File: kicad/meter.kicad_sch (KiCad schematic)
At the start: 10 parts, among them U10 MAX7219, U9 MAX7219

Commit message: kicad updates
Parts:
- added BAR1, BAR2, BAR3, BAR4, BAR5, BAR6, BAR7, BAR8: HDSP-4832_2, Display:HDSP-4832, symbol LED:HDSP-4832_2
- added C1, C12, C13, C2: 100nF, Capacitor_THT:C_Axial_L5.1mm_D3.1mm_P7.50mm_Horizontal, symbol Device:C
- added R1, R2, R3, R4: R, Resistor_THT:R_Axial_DIN0207_L6.3mm_D2.5mm_P10.16mm_Horizontal, symbol Device:R
- added U11: RED, Package_DIP:DIP-24_W7.62mm_Socket, symbol Driver_LED:MAX7219
- added U12: YELLOW, Package_DIP:DIP-24_W7.62mm_Socket, symbol Driver_LED:MAX7219
- U10: value MAX7219 -> GREEN_LOWER; footprint (none) -> Package_DIP:DIP-24_W7.62mm_Socket
- U9: value MAX7219 -> GREEN_UPPER; footprint (none) -> Package_DIP:DIP-24_W7.62mm_Socket
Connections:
- net CLK2 is gone; now on net CLK: U10.13 (CLK)
- net LOAD2 is gone; now on net LOAD: U10.12 (LOAD)
- net +5V: now also C1.2, C12.2, C13.2, C2.2, U11.19 (V+), U12.19 (V+); no longer U10.18 (ISET), U9.18 (ISET)
- net GND: now also C1.1, C12.1, C13.1, C2.1, R1.1, R2.1, R3.1, R4.1, U11.4 (GND), U11.9 (GND), U12.4 (GND), U12.9 (GND); no longer U10.24 (DOUT), U9.24 (DOUT)
- net at U9.20 (SEG_C): now also BAR10.18 (K), BAR11.18 (K), BAR12.18 (K), BAR13.18 (K), BAR14.18 (K), BAR15.18 (K), BAR16.18 (K), BAR9.18 (K)
- net at U9.21 (SEG_E): now also BAR10.16 (K), BAR11.16 (K), BAR12.16 (K), BAR13.16 (K), BAR14.16 (K), BAR15.16 (K), BAR16.16 (K), BAR9.16 (K)
- net at U9.23 (SEG_D): now also BAR10.17 (K), BAR11.17 (K), BAR12.17 (K), BAR13.17 (K), BAR14.17 (K), BAR15.17 (K), BAR16.17 (K), BAR9.17 (K)
- net CLK1 renamed CLK
- net CLK: now also U11.13 (CLK), U12.13 (CLK)
- net DIN1: no longer names the net of U9.1 (DIN)
- net DIN1: now also U12.24 (DOUT)
- net DIN2: no longer names the net of U10.1 (DIN)
- net DIN2: now also U9.24 (DOUT)
- net LOAD1 renamed LOAD
- net LOAD: now also U11.12 (LOAD), U12.12 (LOAD)
- new net: BAR14.10 (A), BAR14.6 (A), BAR14.7 (A), BAR14.8 (A), BAR14.9 (A), U10.10 (DIG_5)
- new net: BAR10.10 (A), BAR10.6 (A), BAR10.7 (A), BAR10.8 (A), BAR10.9 (A), U10.11 (DIG_1)
- new net: BAR10.15 (K), BAR11.15 (K), BAR12.15 (K), BAR13.15 (K), BAR14.15 (K), BAR15.15 (K), BAR16.15 (K), BAR9.15 (K), U10.14 (SEG_A)
- new net: BAR10.14 (K), BAR11.14 (K), BAR12.14 (K), BAR13.14 (K), BAR14.14 (K), BAR15.14 (K), BAR16.14 (K), BAR9.14 (K), U10.16 (SEG_B)
- new net: R2.2, U10.18 (ISET)
- new net: BAR9.10 (A), BAR9.6 (A), BAR9.7 (A), BAR9.8 (A), BAR9.9 (A), U10.2 (DIG_0)
- new net: BAR10.13 (K), BAR11.13 (K), BAR12.13 (K), BAR13.13 (K), BAR14.13 (K), BAR15.13 (K), BAR16.13 (K), BAR9.13 (K), U10.20 (SEG_C)
- new net: BAR10.11 (K), BAR11.11 (K), BAR12.11 (K), BAR13.11 (K), BAR14.11 (K), BAR15.11 (K), BAR16.11 (K), BAR9.11 (K), U10.21 (SEG_E)
- new net: BAR10.12 (K), BAR11.12 (K), BAR12.12 (K), BAR13.12 (K), BAR14.12 (K), BAR15.12 (K), BAR16.12 (K), BAR9.12 (K), U10.23 (SEG_D)
- new net: BAR13.10 (A), BAR13.6 (A), BAR13.7 (A), BAR13.8 (A), BAR13.9 (A), U10.3 (DIG_4)
- new net: BAR15.10 (A), BAR15.6 (A), BAR15.7 (A), BAR15.8 (A), BAR15.9 (A), U10.5 (DIG_6)
- new net: BAR11.10 (A), BAR11.6 (A), BAR11.7 (A), BAR11.8 (A), BAR11.9 (A), U10.6 (DIG_2)
- new net: BAR12.10 (A), BAR12.6 (A), BAR12.7 (A), BAR12.8 (A), BAR12.9 (A), U10.7 (DIG_3)
- new net: BAR16.10 (A), BAR16.6 (A), BAR16.7 (A), BAR16.8 (A), BAR16.9 (A), U10.8 (DIG_7)
- new net: BAR14.1 (A), BAR14.2 (A), BAR14.3 (A), BAR14.4 (A), BAR14.5 (A), U9.10 (DIG_5)
- new net: BAR10.1 (A), BAR10.2 (A), BAR10.3 (A), BAR10.4 (A), BAR10.5 (A), U9.11 (DIG_1)
- new net: BAR10.20 (K), BAR11.20 (K), BAR12.20 (K), BAR13.20 (K), BAR14.20 (K), BAR15.20 (K), BAR16.20 (K), BAR9.20 (K), U9.14 (SEG_A)
- new net: BAR10.19 (K), BAR11.19 (K), BAR12.19 (K), BAR13.19 (K), BAR14.19 (K), BAR15.19 (K), BAR16.19 (K), BAR9.19 (K), U9.16 (SEG_B)
- new net: R1.2, U9.18 (ISET)
- new net: BAR9.1 (A), BAR9.2 (A), BAR9.3 (A), BAR9.4 (A), BAR9.5 (A), U9.2 (DIG_0)
- new net: BAR13.1 (A), BAR13.2 (A), BAR13.3 (A), BAR13.4 (A), BAR13.5 (A), U9.3 (DIG_4)
- new net: BAR15.1 (A), BAR15.2 (A), BAR15.3 (A), BAR15.4 (A), BAR15.5 (A), U9.5 (DIG_6)
- new net: BAR11.1 (A), BAR11.2 (A), BAR11.3 (A), BAR11.4 (A), BAR11.5 (A), U9.6 (DIG_2)
- new net: BAR12.1 (A), BAR12.2 (A), BAR12.3 (A), BAR12.4 (A), BAR12.5 (A), U9.7 (DIG_3)
- new net: BAR16.1 (A), BAR16.2 (A), BAR16.3 (A), BAR16.4 (A), BAR16.5 (A), U9.8 (DIG_7)
- new net: BAR3.1 (A), BAR3.2 (A), BAR3.3 (A), BAR3.4 (A), BAR3.5 (A), U11.6 (DIG_2)
- new net: BAR3.10 (A), BAR3.6 (A), BAR3.7 (A), BAR3.8 (A), BAR3.9 (A), U12.6 (DIG_2)
- new net: BAR1.11 (K), BAR2.11 (K), BAR3.11 (K), BAR4.11 (K), BAR5.11 (K), BAR6.11 (K), BAR7.11 (K), BAR8.11 (K), U12.21 (SEG_E)
- new net: BAR1.12 (K), BAR2.12 (K), BAR3.12 (K), BAR4.12 (K), BAR5.12 (K), BAR6.12 (K), BAR7.12 (K), BAR8.12 (K), U12.23 (SEG_D)
- new net: BAR1.13 (K), BAR2.13 (K), BAR3.13 (K), BAR4.13 (K), BAR5.13 (K), BAR6.13 (K), BAR7.13 (K), BAR8.13 (K), U12.20 (SEG_C)
- new net: BAR1.14 (K), BAR2.14 (K), BAR3.14 (K), BAR4.14 (K), BAR5.14 (K), BAR6.14 (K), BAR7.14 (K), BAR8.14 (K), U12.16 (SEG_B)
- new net: BAR1.15 (K), BAR2.15 (K), BAR3.15 (K), BAR4.15 (K), BAR5.15 (K), BAR6.15 (K), BAR7.15 (K), BAR8.15 (K), U12.14 (SEG_A)
- new net: BAR1.16 (K), BAR2.16 (K), BAR3.16 (K), BAR4.16 (K), BAR5.16 (K), BAR6.16 (K), BAR7.16 (K), BAR8.16 (K), U11.21 (SEG_E)
- new net: BAR1.17 (K), BAR2.17 (K), BAR3.17 (K), BAR4.17 (K), BAR5.17 (K), BAR6.17 (K), BAR7.17 (K), BAR8.17 (K), U11.23 (SEG_D)
- new net: BAR1.18 (K), BAR2.18 (K), BAR3.18 (K), BAR4.18 (K), BAR5.18 (K), BAR6.18 (K), BAR7.18 (K), BAR8.18 (K), U11.20 (SEG_C)
- new net: BAR1.19 (K), BAR2.19 (K), BAR3.19 (K), BAR4.19 (K), BAR5.19 (K), BAR6.19 (K), BAR7.19 (K), BAR8.19 (K), U11.16 (SEG_B)
- new net: BAR1.20 (K), BAR2.20 (K), BAR3.20 (K), BAR4.20 (K), BAR5.20 (K), BAR6.20 (K), BAR7.20 (K), BAR8.20 (K), U11.14 (SEG_A)
- new net: R4.2, U12.18 (ISET)
- new net: BAR4.1 (A), BAR4.2 (A), BAR4.3 (A), BAR4.4 (A), BAR4.5 (A), U11.7 (DIG_3)
- new net: BAR4.10 (A), BAR4.6 (A), BAR4.7 (A), BAR4.8 (A), BAR4.9 (A), U12.7 (DIG_3)
- new net: BAR6.1 (A), BAR6.2 (A), BAR6.3 (A), BAR6.4 (A), BAR6.5 (A), U11.10 (DIG_5)
- new net: BAR6.10 (A), BAR6.6 (A), BAR6.7 (A), BAR6.8 (A), BAR6.9 (A), U12.10 (DIG_5)
- new net: BAR2.1 (A), BAR2.2 (A), BAR2.3 (A), BAR2.4 (A), BAR2.5 (A), U11.11 (DIG_1)
- new net: R3.2, U11.18 (ISET)
- new net: BAR1.1 (A), BAR1.2 (A), BAR1.3 (A), BAR1.4 (A), BAR1.5 (A), U11.2 (DIG_0)
- new net: U11.24 (DOUT), U12.1 (DIN)
- new net: BAR5.1 (A), BAR5.2 (A), BAR5.3 (A), BAR5.4 (A), BAR5.5 (A), U11.3 (DIG_4)
- new net: BAR7.1 (A), BAR7.2 (A), BAR7.3 (A), BAR7.4 (A), BAR7.5 (A), U11.5 (DIG_6)
- new net: BAR8.1 (A), BAR8.2 (A), BAR8.3 (A), BAR8.4 (A), BAR8.5 (A), U11.8 (DIG_7)
- new net: BAR2.10 (A), BAR2.6 (A), BAR2.7 (A), BAR2.8 (A), BAR2.9 (A), U12.11 (DIG_1)
- new net: BAR1.10 (A), BAR1.6 (A), BAR1.7 (A), BAR1.8 (A), BAR1.9 (A), U12.2 (DIG_0)
- new net: BAR5.10 (A), BAR5.6 (A), BAR5.7 (A), BAR5.8 (A), BAR5.9 (A), U12.3 (DIG_4)
- new net: BAR7.10 (A), BAR7.6 (A), BAR7.7 (A), BAR7.8 (A), BAR7.9 (A), U12.5 (DIG_6)
- new net: BAR8.10 (A), BAR8.6 (A), BAR8.7 (A), BAR8.8 (A), BAR8.9 (A), U12.8 (DIG_7)
- new net DIN: U11.1 (DIN)
- now unconnected: U10.15 (SEG_F), U10.17 (SEG_G), U10.22 (SEG_DP)
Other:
- moved on the sheet: BAR10, BAR11, BAR12, BAR13, BAR14, BAR15, BAR16, BAR9, U10, U9

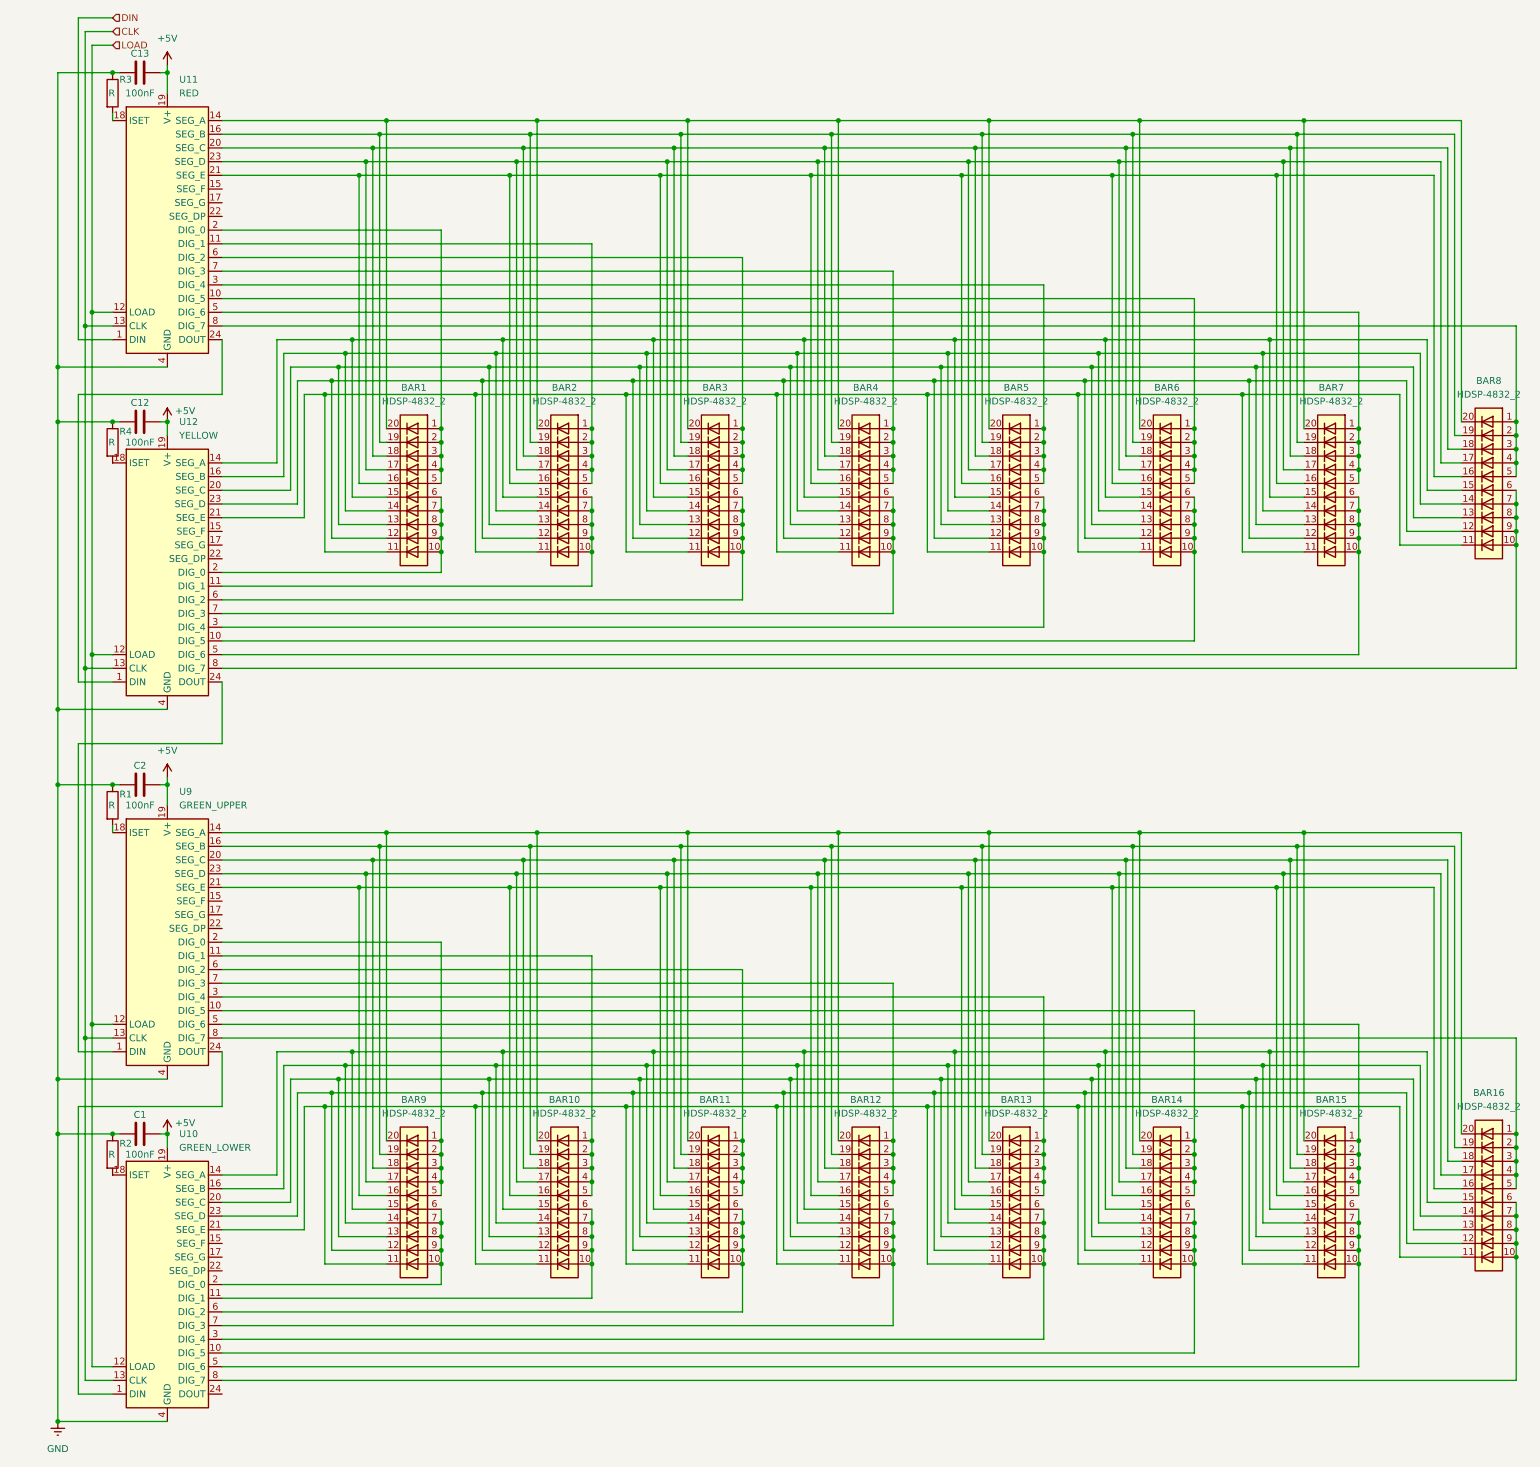
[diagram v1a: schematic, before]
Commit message: pcb routing 1
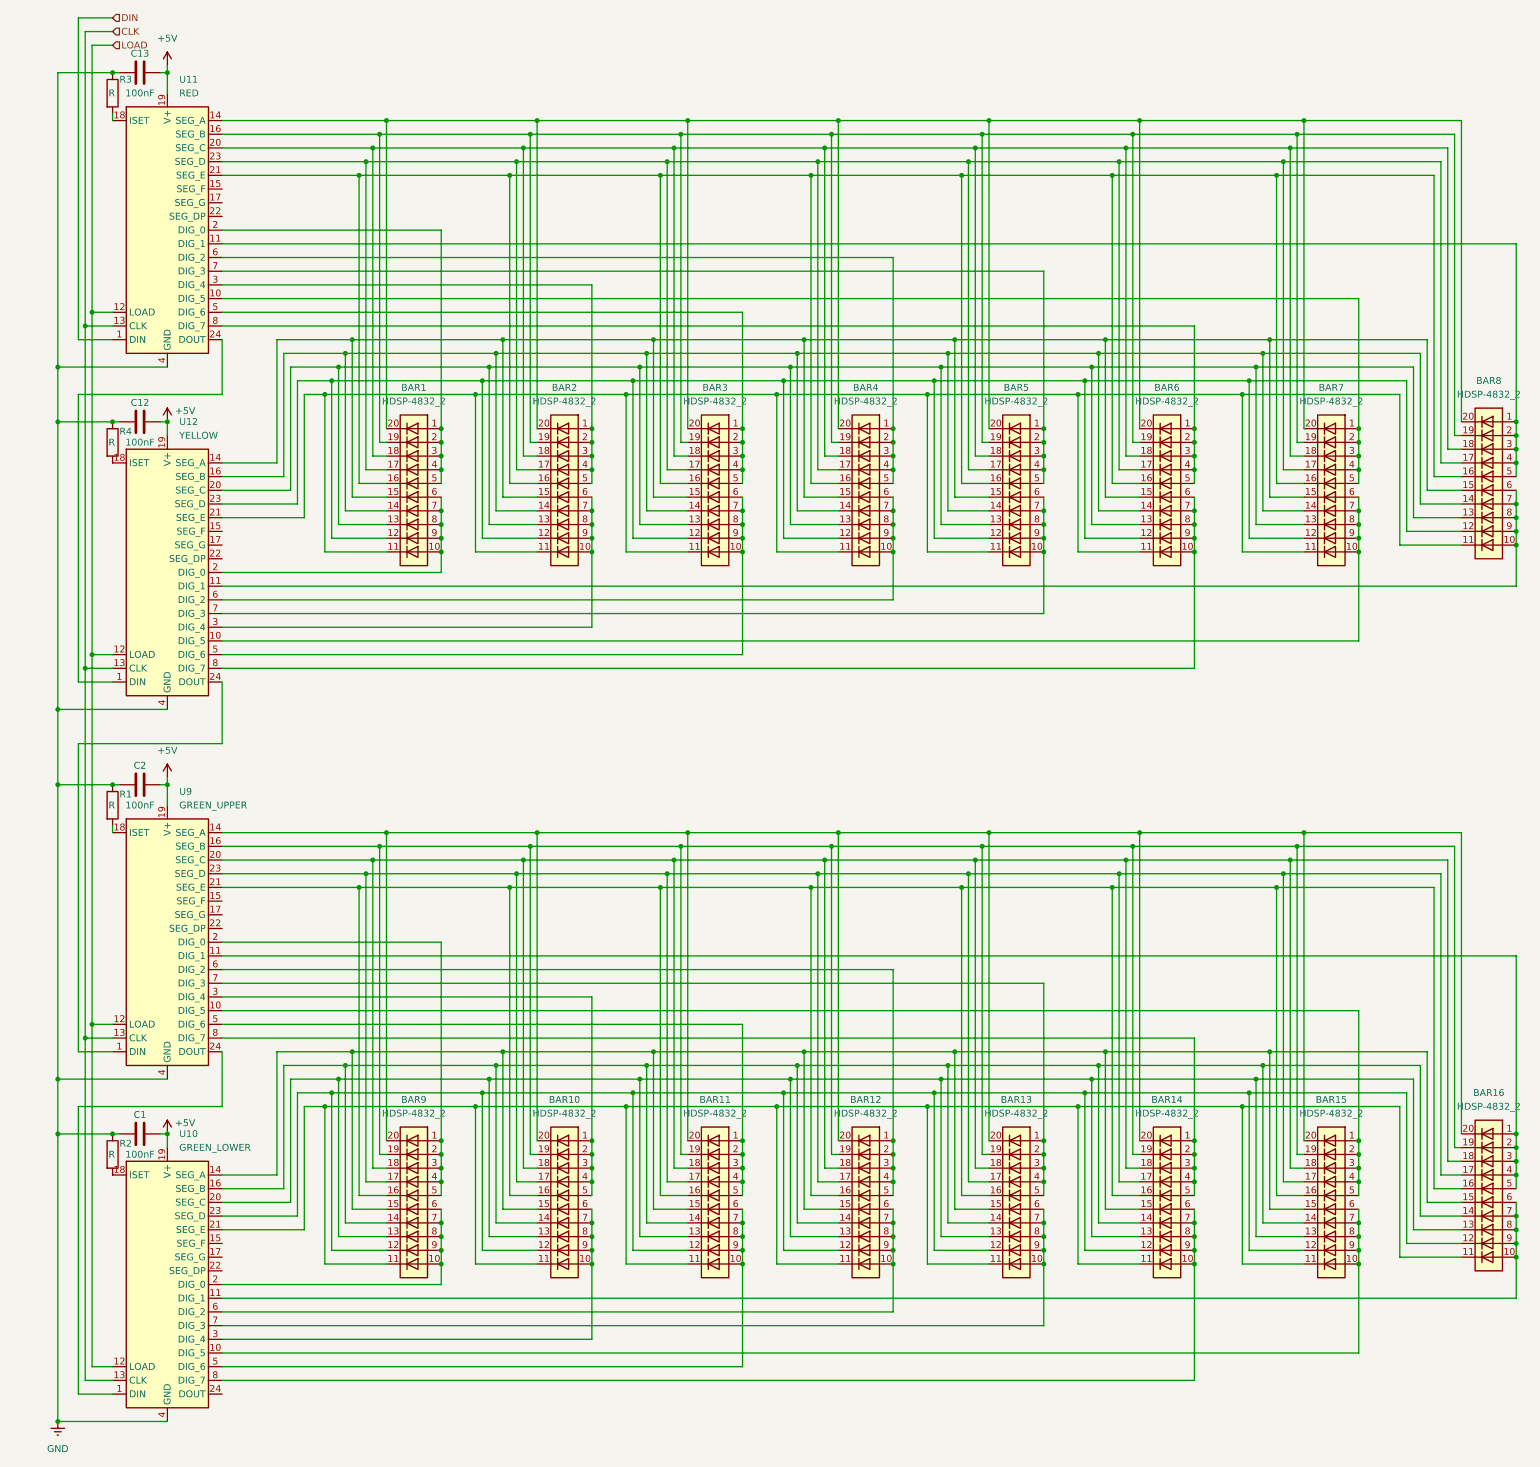
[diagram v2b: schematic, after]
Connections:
- net at BAR14.10 (A), BAR14.6 (A), BAR14.7 (A)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: now also U10.8 (DIG_7); no longer U10.10 (DIG_5)
- net at BAR10.10 (A), BAR10.6 (A), BAR10.7 (A)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: now also U10.3 (DIG_4); no longer U10.11 (DIG_1)
- net at BAR13.10 (A), BAR13.6 (A), BAR13.7 (A)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: now also U10.7 (DIG_3); no longer U10.3 (DIG_4)
- net at BAR15.10 (A), BAR15.6 (A), BAR15.7 (A)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: now also U10.10 (DIG_5); no longer U10.5 (DIG_6)
- net at BAR11.10 (A), BAR11.6 (A), BAR11.7 (A)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: now also U10.5 (DIG_6); no longer U10.6 (DIG_2)
- net at BAR12.10 (A), BAR12.6 (A), BAR12.7 (A)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: now also U10.6 (DIG_2); no longer U10.7 (DIG_3)
- net at BAR16.10 (A), BAR16.6 (A), BAR16.7 (A)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: now also U10.11 (DIG_1); no longer U10.8 (DIG_7)
- net at BAR14.1 (A), BAR14.2 (A), BAR14.3 (A)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: now also U9.8 (DIG_7); no longer U9.10 (DIG_5)
- net at BAR10.1 (A), BAR10.2 (A), BAR10.3 (A)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: now also U9.3 (DIG_4); no longer U9.11 (DIG_1)
- net at BAR13.1 (A), BAR13.2 (A), BAR13.3 (A)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: now also U9.7 (DIG_3); no longer U9.3 (DIG_4)
- net at BAR15.1 (A), BAR15.2 (A), BAR15.3 (A)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: now also U9.10 (DIG_5); no longer U9.5 (DIG_6)
- net at BAR11.1 (A), BAR11.2 (A), BAR11.3 (A)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: now also U9.5 (DIG_6); no longer U9.6 (DIG_2)
- net at BAR12.1 (A), BAR12.2 (A), BAR12.3 (A)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: now also U9.6 (DIG_2); no longer U9.7 (DIG_3)
- net at BAR16.1 (A), BAR16.2 (A), BAR16.3 (A)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: now also U9.11 (DIG_1); no longer U9.8 (DIG_7)
- net at BAR3.1 (A), BAR3.2 (A), BAR3.3 (A)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: now also U11.5 (DIG_6); no longer U11.6 (DIG_2)
- net at BAR3.10 (A), BAR3.6 (A), BAR3.7 (A)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: now also U12.5 (DIG_6); no longer U12.6 (DIG_2)
- net at BAR4.1 (A), BAR4.2 (A), BAR4.3 (A)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: now also U11.6 (DIG_2); no longer U11.7 (DIG_3)
- net at BAR4.10 (A), BAR4.6 (A), BAR4.7 (A)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: now also U12.6 (DIG_2); no longer U12.7 (DIG_3)
- net at BAR6.1 (A), BAR6.2 (A), BAR6.3 (A)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: now also U11.8 (DIG_7); no longer U11.10 (DIG_5)
- net at BAR6.10 (A), BAR6.6 (A), BAR6.7 (A)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: now also U12.8 (DIG_7); no longer U12.10 (DIG_5)
- net at BAR2.1 (A), BAR2.2 (A), BAR2.3 (A)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: now also U11.3 (DIG_4); no longer U11.11 (DIG_1)
- net at BAR5.1 (A), BAR5.2 (A), BAR5.3 (A)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: now also U11.7 (DIG_3); no longer U11.3 (DIG_4)
- net at BAR7.1 (A), BAR7.2 (A), BAR7.3 (A)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: now also U11.10 (DIG_5); no longer U11.5 (DIG_6)
- net at BAR8.1 (A), BAR8.2 (A), BAR8.3 (A)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: now also U11.11 (DIG_1); no longer U11.8 (DIG_7)
- net at BAR2.10 (A), BAR2.6 (A), BAR2.7 (A)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: now also U12.3 (DIG_4); no longer U12.11 (DIG_1)
- net at BAR5.10 (A), BAR5.6 (A), BAR5.7 (A)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: now also U12.7 (DIG_3); no longer U12.3 (DIG_4)
- net at BAR7.10 (A), BAR7.6 (A), BAR7.7 (A)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: now also U12.10 (DIG_5); no longer U12.5 (DIG_6)
- net at BAR8.10 (A), BAR8.6 (A), BAR8.7 (A)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: now also U12.11 (DIG_1); no longer U12.8 (DIG_7)
